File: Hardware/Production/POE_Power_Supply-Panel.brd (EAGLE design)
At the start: 127 x 177.8 mm, 350 parts, among them J1 MAGJACK_SYM, J10 MAGJACK_SYM, J11 USB_A_SMT_FEMALE_NS, J13 MAGJACK_SYM, J14 USB_A_SMT_FEMALE_NS, J16 MAGJACK_SYM, J17 USB_A_SMT_FEMALE_NS, J19 MAGJACK_SYM, J2 USB_A_SMT_FEMALE_NS, J20 USB_A_SMT_FEMALE_NS, J22 MAGJACK_SYM, J23 USB_A_SMT_FEMALE_NS, J4 MAGJACK_SYM, J5 USB_A_SMT_FEMALE_NS, J7 MAGJACK_SYM, J8 USB_A_SMT_FEMALE_NS, U1 POE_PSU-DP990X, U10 POE_PSU-DP990X, U11 3.3V, U12 POE_PSU-DP990X, U13 3.3V, U14 POE_PSU-DP990X, U15 3.3V, U16 POE_PSU-DP990X, U2 3.3V, U3 POE_PSU-DP990X, U4 3.3V, U5 3.3V, U6 POE_PSU-DP990X, U7 3.3V, U8 POE_PSU-DP990X, U9 3.3V

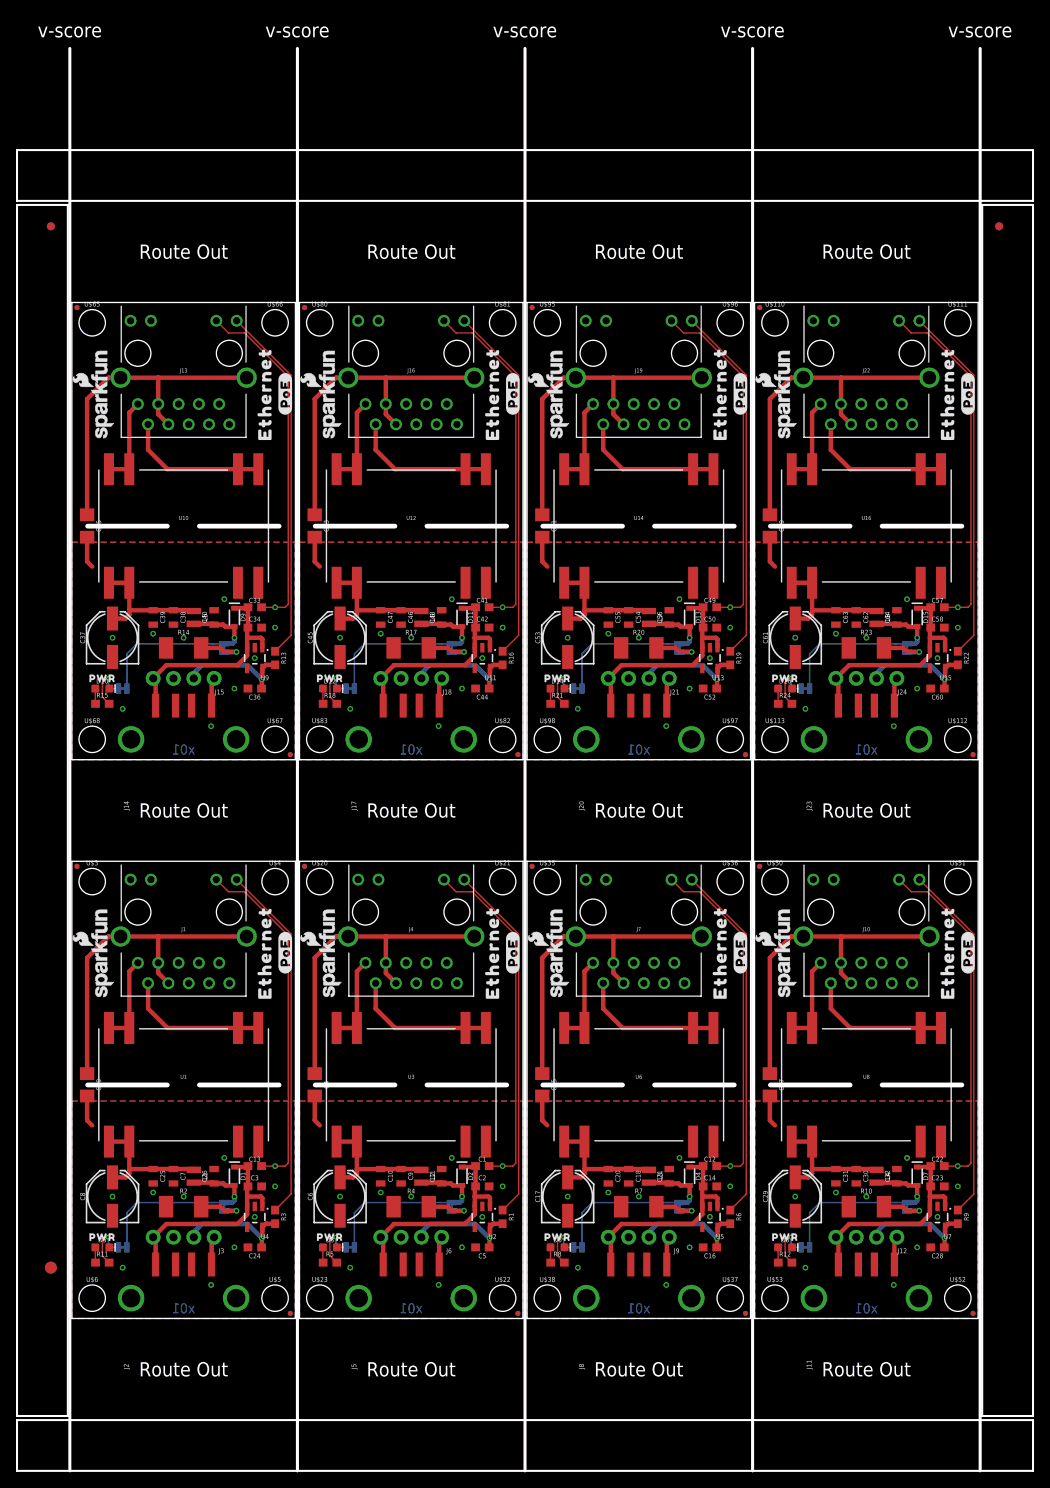
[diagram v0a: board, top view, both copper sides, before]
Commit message: Update x02. Fix FP for load resistor.
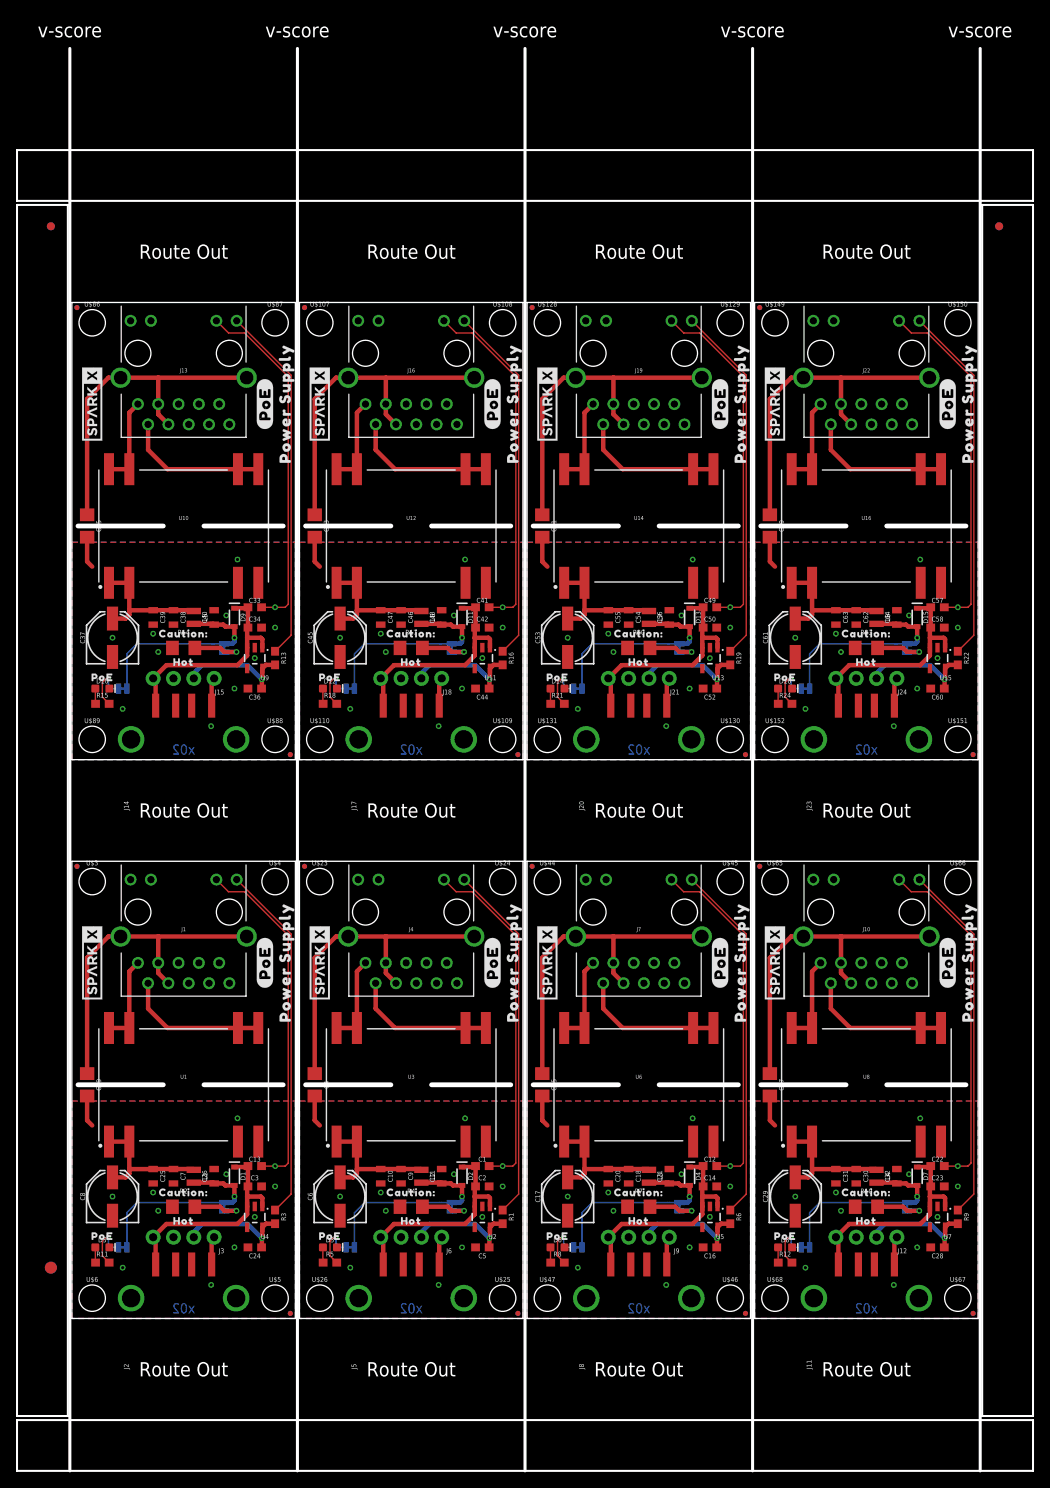
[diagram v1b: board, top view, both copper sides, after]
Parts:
- removed LOGO10, LOGO12, LOGO13, LOGO15, LOGO16, LOGO18, LOGO19, LOGO21, LOGO22, LOGO24, LOGO9: SFE_LOGO_NAME_FLAME.1_INCH, SparkFun-Aesthetics:SFE_LOGO_NAME_FLAME_.1
- removed LOGO11, LOGO14, LOGO17, LOGO20, LOGO23: OSHW-LOGOMINI, SparkFun-Aesthetics:OSHW-LOGO-MINI
- added U$121, U$142, U$163: SPARKX-LOGO4, SparkX:SPARKX-LARGE
- added U$122, U$143, U$164: (no value), output:POWER0
- added U$123, U$144, U$165: (no value), output:SUPPLY1
- added U$124, U$145, U$166: (no value), output:POWER_0
- added U$125, U$146, U$167: (no value), output:SUPPLY_1
- added U$126, U$127, U$147, U$148, U$168: (no value), output:#POE#0
- added U$128, U$129, U$130, U$131, U$149, U$150, U$151, U$152: (no value), SparkFun-Hardware:STAND-OFF
- added U$132, U$153: (no value), output:#LED#0
- added U$133, U$154: (no value), output:#LOAD#0
- added U$134, U$155: (no value), output:#3V3#0
- added U$135, U$156: (no value), output:#5V#2
- added U$136, U$137, U$157, U$158: (no value), output:#GND#1
- added U$138, U$159: (no value), output:CAUTION#0
- added U$139, U$160: (no value), output:HOT1
- added U$140, U$161: (no value), output:POE0
- added U$141, U$162: SPARKX-LOGO4, SparkX:SPARKX-MEDIUM
- J1, J10, J13, J16, J19, J22, J4, J7: value MAGJACK_SYM -> MAGJACK-POE; device Ethernet:MAGJACK-STR_LED -> SparkFun-Connectors:MAGJACK-SYM_LED
- LOAD, LOAD1, LOAD2, LOAD3, LOAD4, LOAD5, LOAD6, LOAD7, POE_LED, POE_LED1, POE_LED2, POE_LED3, POE_LED4, POE_LED5, POE_LED6, POE_LED7: value (none) -> JUMPER-SMT_2_NC_TRACE_SILK
- LOGO1, LOGO2, LOGO4, LOGO6, LOGO7: value SFE_LOGO_NAME_FLAME.1_INCH -> OSHW-LOGOMINI; device SparkFun-Aesthetics:SFE_LOGO_NAME_FLAME_.1 -> SparkFun-Aesthetics:OSHW-LOGO-MINI
- R10, R14, R17, R2, R20, R23, R4, R7: value 510 -> 49.9OHM-1206-1/2W-1%; device SparkFun-Resistors:2010 -> SparkFun-Resistors:1206
- U$1, U$106, U$63: device output:ETHERNET0 -> output:#POE#0
- U$100: value (none) -> SPARKX-LOGO4; device output:#LED#0 -> SparkX:SPARKX-LARGE
- U$101: device output:#LOAD#0 -> output:POWER0
- U$102: device output:#3V3#0 -> output:SUPPLY1
- U$103: device output:#5V#2 -> output:POWER_0
- U$104: device output:#GND#1 -> output:SUPPLY_1
- U$105: device output:#GND#1 -> output:#POE#0
- U$107, U$109, U$47: device output:#POE#0 -> SparkFun-Hardware:STAND-OFF
- U$108, U$46: device output:ETHERNET0 -> SparkFun-Hardware:STAND-OFF
- U$111: device SparkFun-Hardware:STAND-OFF -> output:#LED#0
- U$112: device SparkFun-Hardware:STAND-OFF -> output:#LOAD#0
- U$113, U$50: device SparkFun-Hardware:STAND-OFF -> output:#3V3#0
- U$114: device output:PWR0 -> output:#5V#2
- U$115: device output:#LED#0 -> output:#GND#1
- U$116: device output:#LOAD#0 -> output:#GND#1
- U$117: device output:#3V3#0 -> output:CAUTION#0
- U$118: device output:#5V#2 -> output:HOT1
- U$119: device output:#GND#1 -> output:POE0
- U$120: value (none) -> SPARKX-LOGO4; device output:#GND#1 -> SparkX:SPARKX-MEDIUM
- U$14, U$33: device output:ETHERNET0 -> output:CAUTION#0
- U$15, U$34: device output:#POE#0 -> output:HOT1
- U$16: device output:ETHERNET0 -> output:POE0
- U$17, U$61: device output:ETHERNET0 -> output:POWER_0
- U$19, U$79: value (none) -> SPARKX-LOGO4; device output:#POE#0 -> SparkX:SPARKX-LARGE
- U$20, U$38, U$80: device SparkFun-Hardware:STAND-OFF -> output:POWER0
- U$21, U$81: device SparkFun-Hardware:STAND-OFF -> output:SUPPLY1
- U$22, U$83: device SparkFun-Hardware:STAND-OFF -> output:SUPPLY_1
- U$24: device output:PWR0 -> SparkFun-Hardware:STAND-OFF
- U$25: device output:#LED#0 -> SparkFun-Hardware:STAND-OFF
- U$26, U$86: device output:#LOAD#0 -> SparkFun-Hardware:STAND-OFF
- U$27: device output:#3V3#0 -> output:#LED#0
- U$28: device output:#5V#2 -> output:#LOAD#0
- U$29: device output:#GND#1 -> output:#3V3#0
- U$30: device output:#GND#1 -> output:#5V#2
- U$31: device output:ETHERNET0 -> output:#GND#1
- U$32, U$94: device output:#POE#0 -> output:#GND#1
- U$35, U$98: device SparkFun-Hardware:STAND-OFF -> output:POE0
- U$36: value (none) -> SPARKX-LOGO4; device SparkFun-Hardware:STAND-OFF -> SparkX:SPARKX-MEDIUM
- U$37: value (none) -> SPARKX-LOGO4; device SparkFun-Hardware:STAND-OFF -> SparkX:SPARKX-LARGE
- U$39: device output:PWR0 -> output:SUPPLY1
- U$40: device output:#LED#0 -> output:POWER_0
- U$41: device output:#LOAD#0 -> output:SUPPLY_1
- U$42: device output:#3V3#0 -> output:#POE#0
- U$43: device output:#5V#2 -> output:#POE#0
- U$44, U$45, U$89: device output:#GND#1 -> SparkFun-Hardware:STAND-OFF
- U$48: device output:ETHERNET0 -> output:#LED#0
- U$49: device output:#POE#0 -> output:#LOAD#0
- U$51: device SparkFun-Hardware:STAND-OFF -> output:#5V#2
- U$52, U$53, U$95: device SparkFun-Hardware:STAND-OFF -> output:#GND#1
- U$54: device output:PWR0 -> output:CAUTION#0
- U$55: device output:#LED#0 -> output:HOT1
- U$56: device output:#LOAD#0 -> output:POE0
- U$57: value (none) -> SPARKX-LOGO4; device output:#3V3#0 -> SparkX:SPARKX-MEDIUM
- U$58: value (none) -> SPARKX-LOGO4; device output:#5V#2 -> SparkX:SPARKX-LARGE
- U$59: device output:#GND#1 -> output:POWER0
- U$60: device output:#GND#1 -> output:SUPPLY1
- U$62: device output:#POE#0 -> output:SUPPLY_1
- U$69: device output:PWR0 -> output:#LED#0
- U$7, U$99: value (none) -> SPARKX-LOGO4; device output:PWR0 -> SparkX:SPARKX-MEDIUM
- U$70: device output:#LED#0 -> output:#LOAD#0
- U$71: device output:#LOAD#0 -> output:#3V3#0
- U$72: device output:#3V3#0 -> output:#5V#2
- U$73: device output:#5V#2 -> output:#GND#1
- U$75: device output:#GND#1 -> output:CAUTION#0
- U$76: device output:ETHERNET0 -> output:HOT1
- U$77: device output:#POE#0 -> output:POE0
- U$78: value (none) -> SPARKX-LOGO4; device output:ETHERNET0 -> SparkX:SPARKX-MEDIUM
- U$82: device SparkFun-Hardware:STAND-OFF -> output:POWER_0
- U$84: device output:PWR0 -> output:#POE#0
- U$85: device output:#LED#0 -> output:#POE#0
- U$87: device output:#3V3#0 -> SparkFun-Hardware:STAND-OFF
- U$88: device output:#5V#2 -> SparkFun-Hardware:STAND-OFF
- U$90: device output:#GND#1 -> output:#LED#0
- U$91: device output:ETHERNET0 -> output:#LOAD#0
- U$92: device output:#POE#0 -> output:#3V3#0
- U$93: device output:ETHERNET0 -> output:#5V#2
- U$96: device SparkFun-Hardware:STAND-OFF -> output:CAUTION#0
- U$97: device SparkFun-Hardware:STAND-OFF -> output:HOT1
- U1, U10, U12, U14, U16, U3, U6, U8: device Ethernet:DP990X -> SparkFun-IC-Power:DP990X
- moved U$70 121.5 mm to (108.0, 14.0)
- moved U$80 116.7 mm to (112.0, 40.5), turned to 90 degrees
- moved U$74 114.3 mm to (103.1, 7.37)
- moved U$76 113.5 mm to (99.3, 12.2), turned to 0 degrees
- moved U$73 112.6 mm to (98.0, 7.37)
- moved U$69 111.9 mm to (91.7, 10.8), flipped to the bottom
- moved U$77 110.6 mm to (89.2, 10.3), turned to 0 degrees
- moved U$65 110.3 mm to (87.9, 54.6)
- moved U$66 110.3 mm to (110.7, 54.6)
- moved U$67 110.3 mm to (110.7, 2.54)
- moved U$68 110.3 mm to (87.9, 2.54)
- moved U$71 109.1 mm to (100.6, 7.49), turned to 270 degrees
- moved U$72 106.2 mm to (95.5, 7.87)
- moved U$62 104.8 mm to (70.4, 20.3), flipped to the bottom, turned to 0 degrees
- moved U$64 104.6 mm to (109.5, 44.5), flipped to the top, turned to 90 degrees
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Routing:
- net N$22: track 6.14 -> 6.94 mm
- net N$2: track 6.14 -> 6.94 mm
- net N$9: track 6.14 -> 6.94 mm
- net N$18: track 6.14 -> 6.94 mm
- net N$8: track 6.14 -> 6.94 mm
- net N$30: track 6.14 -> 6.94 mm
- net N$26: track 6.14 -> 6.94 mm
- net N$14: track 6.14 -> 6.94 mm
- net GND7: vias 10 -> 11
- net GND6: vias 10 -> 11
- net GND5: vias 10 -> 11
- net GND4: vias 10 -> 11
- net GND3: vias 10 -> 11
- net GND2: vias 10 -> 11
- net GND1: vias 10 -> 11
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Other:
- outline, holes or cut-outs redrawn
- board text added: "x02"
- board text removed: "x01"
